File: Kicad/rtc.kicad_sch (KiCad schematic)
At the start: 8 parts, among them Y18001 32,768 Hz

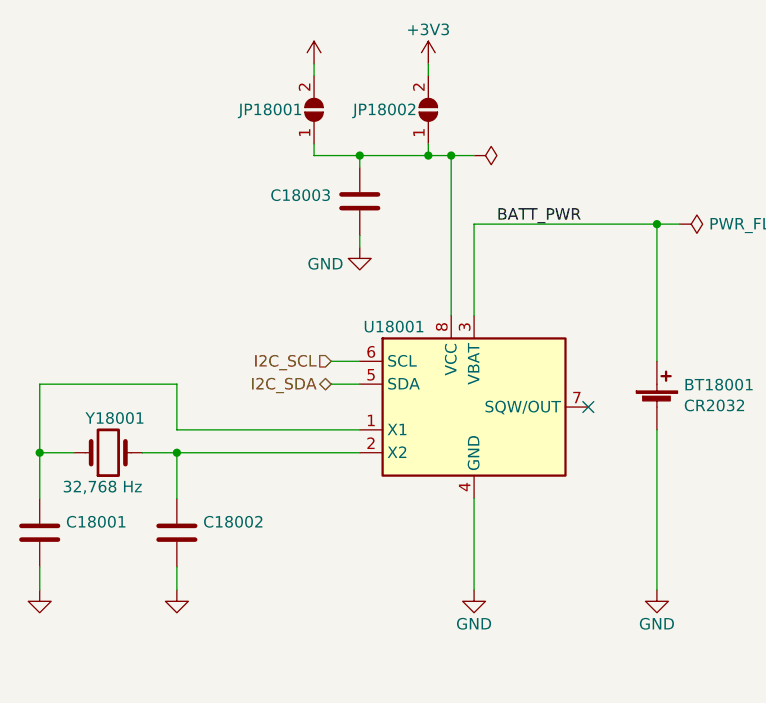
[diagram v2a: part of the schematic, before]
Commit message: Set missing footprints and update PCB
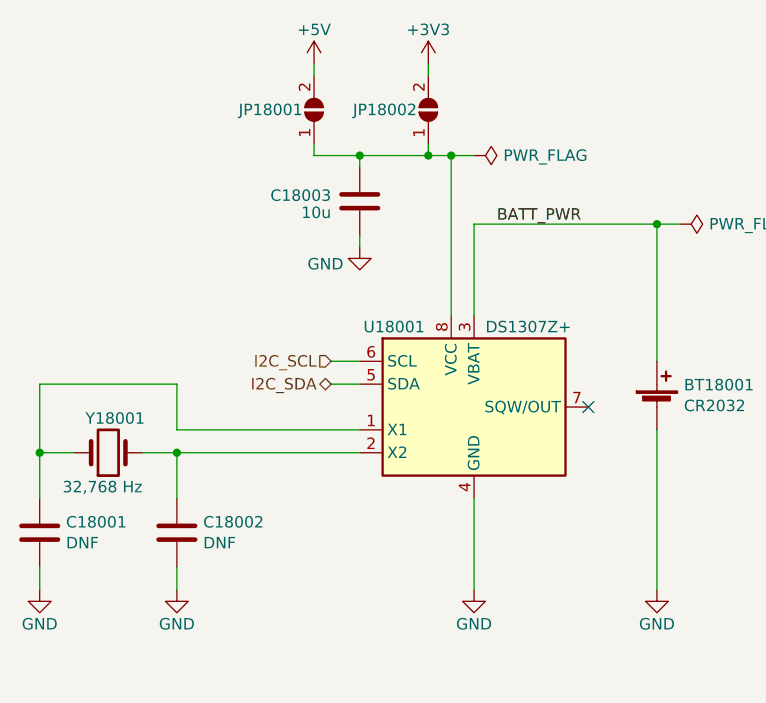
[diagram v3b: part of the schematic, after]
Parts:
- C18001, C18002: value (none) -> DNF; footprint (none) -> Capacitor_SMD:C_0805_2012Metric_Pad1.18x1.45mm_HandSolder
- C18003: value (none) -> 10u; footprint (none) -> Capacitor_SMD:C_0805_2012Metric_Pad1.18x1.45mm_HandSolder; JLCPCB Collection Basic -> (none); LCSC Part# C15850 -> (none); MPN CL21A106KAYNNNE -> (none); Manufacturer Samsung -> (none)
- JP18001, JP18002: value (none) -> Bridge; footprint (none) -> Jumper:SolderJumper-2_P1.3mm_Open_RoundedPad1.0x1.5mm
- U18001: value (none) -> DS1307Z+; footprint (none) -> Package_SO:SOIC-8_3.9x4.9mm_P1.27mm
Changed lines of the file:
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@@
       (effects (font (size 1.27 1.27)) (justify left))
     )
-    (property "Value" "" (id 1) (at 91.821 106.553 0)
-      (effects (font (size 1.27 1.27)) (justify left))
-    )
-    (property "Footprint" "" (id 2) (at 89.8652 109.22 0)
+    (property "Value" "DNF" (id 1) (at 91.821 106.553 0)
+      (effects (font (size 1.27 1.27)) (justify left))
+    )
+    (property "Footprint" "Capacitor_SMD:C_0805_2012Metric_Pad1.18x1.45mm_HandSolder" (id 2) (at 89.8652 109.22 0)
       (effects (font (size 1.27 1.27)) hide)
     )
@@
       (effects (font (size 1.27 1.27)) hide)
     )
-    (property "Value" "" (id 1) (at 119.38 49.53 0))
+    (property "Value" "+5V" (id 1) (at 119.38 49.53 0))
     (property "Footprint" "" (id 2) (at 119.38 53.34 0)
       (effects (font (size 1.27 1.27)) hide)
@@
       (effects (font (size 1.27 1.27)) hide)
     )
-    (property "Value" "" (id 1) (at 104.14 115.57 0))
+    (property "Value" "GND" (id 1) (at 104.14 115.57 0))
     (property "Footprint" "" (id 2) (at 104.14 111.76 0)
       (effects (font (size 1.27 1.27)) hide)
@@
       (effects (font (size 1.27 1.27)) (justify left))
     )
-    (property "Value" "" (id 1) (at 128.27 58.42 0)
-      (effects (font (size 1.27 1.27)) hide)
-    )
-    (property "Footprint" "" (id 2) (at 132.08 58.42 0)
+    (property "Value" "Bridge" (id 1) (at 128.27 58.42 0)
+      (effects (font (size 1.27 1.27)) hide)
+    )
+    (property "Footprint" "Jumper:SolderJumper-2_P1.3mm_Open_RoundedPad1.0x1.5mm" (id 2) (at 132.08 58.42 0)
       (effects (font (size 1.27 1.27)) hide)
     )
@@
       (effects (font (size 1.27 1.27)) hide)
     )
-    (property "Value" "" (id 1) (at 140.4112 63.5 90)
+    (property "Value" "PWR_FLAG" (id 1) (at 140.4112 63.5 90)
       (effects (font (size 1.27 1.27)) (justify left))
     )
@@
       (effects (font (size 1.27 1.27)) (justify left))
     )
-    (property "Value" "" (id 1) (at 115.57 58.42 0)
-      (effects (font (size 1.27 1.27)) hide)
-    )
-    (property "Footprint" "" (id 2) (at 119.38 58.42 0)
+    (property "Value" "Bridge" (id 1) (at 115.57 58.42 0)
+      (effects (font (size 1.27 1.27)) hide)
+    )
+    (property "Footprint" "Jumper:SolderJumper-2_P1.3mm_Open_RoundedPad1.0x1.5mm" (id 2) (at 119.38 58.42 0)
       (effects (font (size 1.27 1.27)) hide)
     )
@@
       (effects (font (size 1.27 1.27)) hide)
     )
-    (property "Value" "" (id 1) (at 88.9 115.57 0))
+    (property "Value" "GND" (id 1) (at 88.9 115.57 0))
     (property "Footprint" "" (id 2) (at 88.9 111.76 0)
       (effects (font (size 1.27 1.27)) hide)
@@
       (effects (font (size 1.27 1.27)) (justify left))
     )
-    (property "Value" "" (id 1) (at 107.061 106.553 0)
-      (effects (font (size 1.27 1.27)) (justify left))
-    )
-    (property "Footprint" "" (id 2) (at 105.1052 109.22 0)
+    (property "Value" "DNF" (id 1) (at 107.061 106.553 0)
+      (effects (font (size 1.27 1.27)) (justify left))
+    )
+    (property "Footprint" "Capacitor_SMD:C_0805_2012Metric_Pad1.18x1.45mm_HandSolder" (id 2) (at 105.1052 109.22 0)
       (effects (font (size 1.27 1.27)) hide)
     )
@@
       (effects (font (size 1.27 1.27)) (justify right))
     )
-    (property "Value" "" (id 1) (at 121.285 69.85 0)
+    (property "Value" "10u" (id 1) (at 121.285 69.85 0)
       (effects (font (size 1.27 1.27)) (justify right))
     )
-    (property "Footprint" "" (id 2) (at 125.4252 64.77 0)
+    (property "Footprint" "Capacitor_SMD:C_0805_2012Metric_Pad1.18x1.45mm_HandSolder" (id 2) (at 125.4252 64.77 0)
       (effects (font (size 1.27 1.27)) hide)
     )
@@
       (effects (font (size 1.27 1.27)) hide)
     )
-    (property "Digikey" "~" (id 5) (at 124.46 68.58 0)
-      (effects (font (size 1.27 1.27)) hide)
-    )
-    (property "MPN" "CL21A106KAYNNNE" (id 6) (at 124.46 68.58 0)
-      (effects (font (size 1.27 1.27)) hide)
-    )
-    (property "Manufacturer" "Samsung" (id 7) (at 124.46 68.58 0)
-      (effects (font (size 1.27 1.27)) hide)
-    )
-    (property "LCSC Part#" "C15850" (id 8) (at 124.46 68.58 0)
+    (property "Digikey" "" (id 5) (at 124.46 68.58 0)
+      (effects (font (size 1.27 1.27)) hide)
+    )
+    (property "MPN" "" (id 6) (at 124.46 68.58 0)
+      (effects (font (size 1.27 1.27)) hide)
+    )
+    (property "Manufacturer" "" (id 7) (at 124.46 68.58 0)
+      (effects (font (size 1.27 1.27)) hide)
+    )
+    (property "LCSC Part#" "" (id 8) (at 124.46 68.58 0)
       (effects (font (size 1.27 1.27)) hide)
     )
@@
       (effects (font (size 1.27 1.27)) hide)
     )
-    (property "Mouser" "~" (id 11) (at 124.46 68.58 0)
-      (effects (font (size 1.27 1.27)) hide)
-    )
-    (property "JLCPCB Collection" "Basic" (id 12) (at 124.46 68.58 0)
+    (property "Mouser" "" (id 11) (at 124.46 68.58 0)
+      (effects (font (size 1.27 1.27)) hide)
+    )
+    (property "JLCPCB Collection" "" (id 12) (at 124.46 68.58 0)
       (effects (font (size 1.27 1.27)) hide)
     )
@@
     (in_bom yes) (on_board yes)
     (property "Reference" "U18001" (id 0) (at 128.27 82.55 0))
-    (property "Value" "" (id 1) (at 138.43 82.55 0)
-      (effects (font (size 1.27 1.27)) (justify left))
-    )
-    (property "Footprint" "" (id 2) (at 137.16 104.14 0)
-      (effects (font (size 1.27 1.27)) hide)
-    )
+    (property "Value" "DS1307Z+" (id 1) (at 138.43 82.55 0)
+      (effects (font (size 1.27 1.27)) (justify left))
+    )
+    (property "Footprint" "Package_SO:SOIC-8_3.9x4.9mm_P1.27mm" (id 2) (at 137.16 104.14 0)
+      (effects (font (size 1.27 1.27)) hide)
+    )

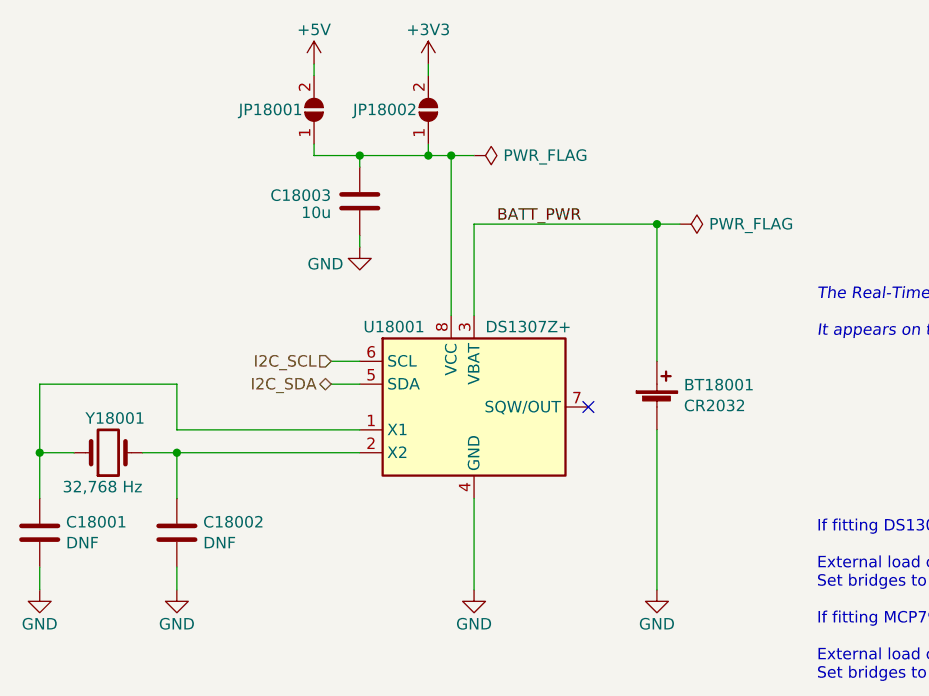
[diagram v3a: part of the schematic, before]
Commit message: Re-imported from Neotron Pico v1.1.
This time I deleted the sheets from the top level and then re-added pointing at the new files. I also reset the PCB dimensions to match the Neotron Pico.

This seems to have done a better job importing footprints.
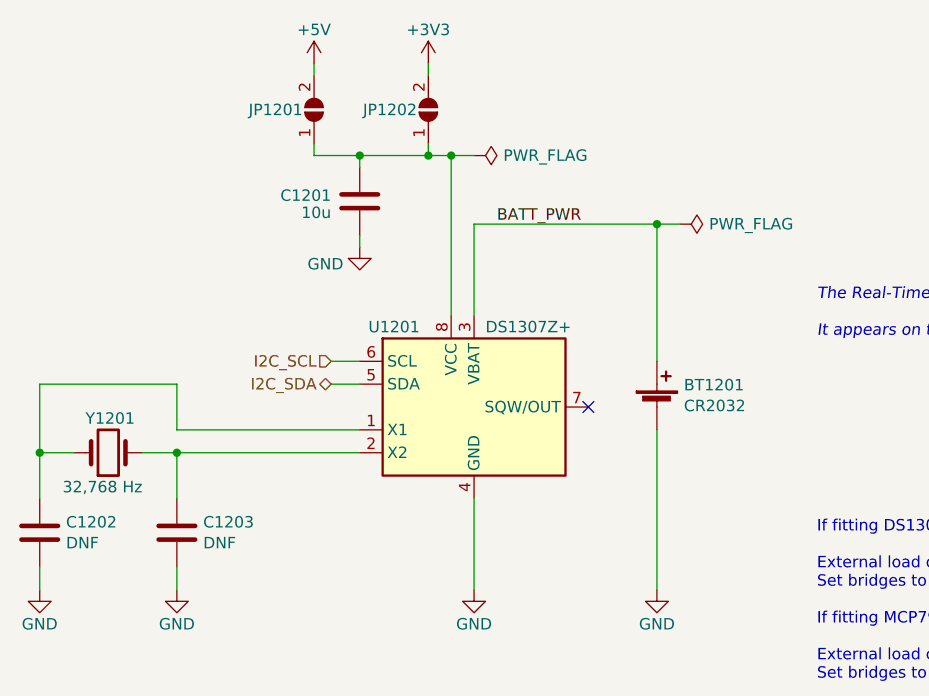
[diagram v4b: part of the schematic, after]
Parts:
- C1201: renamed from C18003; JLCPCB Collection (none) -> Basic; LCSC Part# (none) -> C15850; MPN (none) -> CL21A106KAYNNNE; Manufacturer (none) -> Samsung
- Y1201: renamed from Y18001; footprint Crystal:Crystal_DS26_D2.0mm_L6.0mm_Horizontal -> Crystal:Crystal_SMD_3215-2Pin_3.2x1.5mm
- renumbered BT18001 to BT1201, C18001 to C1202, C18002 to C1203, JP18001 to JP1201, JP18002 to JP1202, U18001 to U1201
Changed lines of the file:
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@@
   (symbol (lib_id "power:GND") (at 124.46 73.66 0) (unit 1)
     (in_bom yes) (on_board yes)
-    (property "Reference" "#PWR018004" (id 0) (at 124.46 80.01 0)
+    (property "Reference" "#PWR01203" (id 0) (at 124.46 80.01 0)
       (effects (font (size 1.27 1.27)) hide)
     )
@@
   (symbol (lib_id "power:+3V3") (at 132.08 53.34 0) (unit 1)
     (in_bom yes) (on_board yes)
-    (property "Reference" "#PWR018005" (id 0) (at 132.08 57.15 0)
+    (property "Reference" "#PWR01202" (id 0) (at 132.08 57.15 0)
       (effects (font (size 1.27 1.27)) hide)
     )
@@
   (symbol (lib_id "power:GND") (at 137.16 111.76 0) (unit 1)
     (in_bom yes) (on_board yes)
-    (property "Reference" "#PWR018006" (id 0) (at 137.16 118.11 0)
+    (property "Reference" "#PWR01206" (id 0) (at 137.16 118.11 0)
       (effects (font (size 1.27 1.27)) hide)
     )
@@
   (symbol (lib_id "Device:Crystal") (at 96.52 96.52 0) (mirror x) (unit 1)
     (in_bom yes) (on_board yes)
-    (property "Reference" "Y18001" (id 0) (at 93.98 92.71 0)
+    (property "Reference" "Y1201" (id 0) (at 93.98 92.71 0)
       (effects (font (size 1.27 1.27)) (justify left))
     )
@@
       (effects (font (size 1.27 1.27)) (justify left))
     )
-    (property "Footprint" "Crystal:Crystal_DS26_D2.0mm_L6.0mm_Horizontal" (id 2) (at 96.52 96.52 0)
+    (property "Footprint" "Crystal:Crystal_SMD_3215-2Pin_3.2x1.5mm" (id 2) (at 96.52 96.52 0)
       (effects (font (size 1.27 1.27)) hide)
     )
@@
   (symbol (lib_id "power:GND") (at 157.48 111.76 0) (unit 1)
     (in_bom yes) (on_board yes)
-    (property "Reference" "#PWR018007" (id 0) (at 157.48 118.11 0)
+    (property "Reference" "#PWR01207" (id 0) (at 157.48 118.11 0)
       (effects (font (size 1.27 1.27)) hide)
     )
@@
   (symbol (lib_id "Device:Battery_Cell") (at 157.48 91.44 0) (unit 1)
     (in_bom yes) (on_board yes)
-    (property "Reference" "BT18001" (id 0) (at 160.4772 89.0016 0)
+    (property "Reference" "BT1201" (id 0) (at 160.4772 89.0016 0)
       (effects (font (size 1.27 1.27)) (justify left))
     )
@@
   (symbol (lib_id "power:PWR_FLAG") (at 160.02 71.12 270) (unit 1)
     (in_bom yes) (on_board yes)
-    (property "Reference" "#FLG018002" (id 0) (at 161.925 71.12 0)
+    (property "Reference" "#FLG01202" (id 0) (at 161.925 71.12 0)
       (effects (font (size 1.27 1.27)) hide)
     )
@@
   (symbol (lib_id "Device:C") (at 88.9 105.41 0) (unit 1)
     (in_bom yes) (on_board yes)
-    (property "Reference" "C18001" (id 0) (at 91.821 104.2416 0)
+    (property "Reference" "C1202" (id 0) (at 91.821 104.2416 0)
       (effects (font (size 1.27 1.27)) (justify left))
     )
@@
   (symbol (lib_id "power:+5V") (at 119.38 53.34 0) (unit 1)
     (in_bom yes) (on_board yes)
-    (property "Reference" "#PWR018003" (id 0) (at 119.38 57.15 0)
+    (property "Reference" "#PWR01201" (id 0) (at 119.38 57.15 0)
       (effects (font (size 1.27 1.27)) hide)
     )
@@
   (symbol (lib_id "power:GND") (at 104.14 111.76 0) (unit 1)
     (in_bom yes) (on_board yes)
-    (property "Reference" "#PWR018002" (id 0) (at 104.14 118.11 0)
+    (property "Reference" "#PWR01205" (id 0) (at 104.14 118.11 0)
       (effects (font (size 1.27 1.27)) hide)
     )
@@
   (symbol (lib_id "Jumper:SolderJumper_2_Open") (at 132.08 58.42 90) (unit 1)
     (in_bom yes) (on_board yes)
-    (property "Reference" "JP18002" (id 0) (at 130.81 58.42 90)
+    (property "Reference" "JP1202" (id 0) (at 130.81 58.42 90)
       (effects (font (size 1.27 1.27)) (justify left))
     )
@@
   (symbol (lib_id "power:PWR_FLAG") (at 137.16 63.5 270) (unit 1)
     (in_bom yes) (on_board yes)
-    (property "Reference" "#FLG018001" (id 0) (at 139.065 63.5 0)
+    (property "Reference" "#FLG01201" (id 0) (at 139.065 63.5 0)
       (effects (font (size 1.27 1.27)) hide)
     )
@@
   (symbol (lib_id "Jumper:SolderJumper_2_Open") (at 119.38 58.42 90) (unit 1)
     (in_bom yes) (on_board yes)
-    (property "Reference" "JP18001" (id 0) (at 118.11 58.42 90)
+    (property "Reference" "JP1201" (id 0) (at 118.11 58.42 90)
       (effects (font (size 1.27 1.27)) (justify left))
     )
@@
   (symbol (lib_id "power:GND") (at 88.9 111.76 0) (unit 1)
     (in_bom yes) (on_board yes)
-    (property "Reference" "#PWR018001" (id 0) (at 88.9 118.11 0)
+    (property "Reference" "#PWR01204" (id 0) (at 88.9 118.11 0)
       (effects (font (size 1.27 1.27)) hide)
     )
@@
   (symbol (lib_id "Device:C") (at 104.14 105.41 0) (unit 1)
     (in_bom yes) (on_board yes)
-    (property "Reference" "C18002" (id 0) (at 107.061 104.2416 0)
+    (property "Reference" "C1203" (id 0) (at 107.061 104.2416 0)
       (effects (font (size 1.27 1.27)) (justify left))
     )
@@
   (symbol (lib_id "Device:C") (at 124.46 68.58 0) (mirror x) (unit 1)
     (in_bom yes) (on_board yes)
-    (property "Reference" "C18003" (id 0) (at 121.285 67.945 0)
+    (property "Reference" "C1201" (id 0) (at 121.285 67.945 0)
       (effects (font (size 1.27 1.27)) (justify right))
     )
@@
       (effects (font (size 1.27 1.27)) hide)
     )
-    (property "Digikey" "" (id 5) (at 124.46 68.58 0)
-      (effects (font (size 1.27 1.27)) hide)
-    )
-    (property "MPN" "" (id 6) (at 124.46 68.58 0)
-      (effects (font (size 1.27 1.27)) hide)
-    )
-    (property "Manufacturer" "" (id 7) (at 124.46 68.58 0)
-      (effects (font (size 1.27 1.27)) hide)
-    )
-    (property "LCSC Part#" "" (id 8) (at 124.46 68.58 0)
+    (property "Digikey" "~" (id 5) (at 124.46 68.58 0)
+      (effects (font (size 1.27 1.27)) hide)
+    )
+    (property "MPN" "CL21A106KAYNNNE" (id 6) (at 124.46 68.58 0)
+      (effects (font (size 1.27 1.27)) hide)
+    )
+    (property "Manufacturer" "Samsung" (id 7) (at 124.46 68.58 0)
+      (effects (font (size 1.27 1.27)) hide)
+    )
+    (property "LCSC Part#" "C15850" (id 8) (at 124.46 68.58 0)
       (effects (font (size 1.27 1.27)) hide)
     )
@@
       (effects (font (size 1.27 1.27)) hide)
     )
-    (property "Mouser" "" (id 11) (at 124.46 68.58 0)
-      (effects (font (size 1.27 1.27)) hide)
-    )
-    (property "JLCPCB Collection" "" (id 12) (at 124.46 68.58 0)
+    (property "Mouser" "~" (id 11) (at 124.46 68.58 0)
+      (effects (font (size 1.27 1.27)) hide)
+    )
+    (property "JLCPCB Collection" "Basic" (id 12) (at 124.46 68.58 0)
       (effects (font (size 1.27 1.27)) hide)
     )
@@
   (symbol (lib_id "Timer_RTC:DS1307Z+") (at 137.16 91.44 0) (unit 1)
     (in_bom yes) (on_board yes)
-    (property "Reference" "U18001" (id 0) (at 128.27 82.55 0))
+    (property "Reference" "U1201" (id 0) (at 128.27 82.55 0))
     (property "Value" "DS1307Z+" (id 1) (at 138.43 82.55 0)
       (effects (font (size 1.27 1.27)) (justify left))
